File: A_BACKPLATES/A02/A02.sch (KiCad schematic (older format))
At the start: 218 parts, among them J0 Conn_01x01_Male, J1 Conn_01x01_Male, J2 Conn_01x01_Male, J3 Conn_01x01_Male

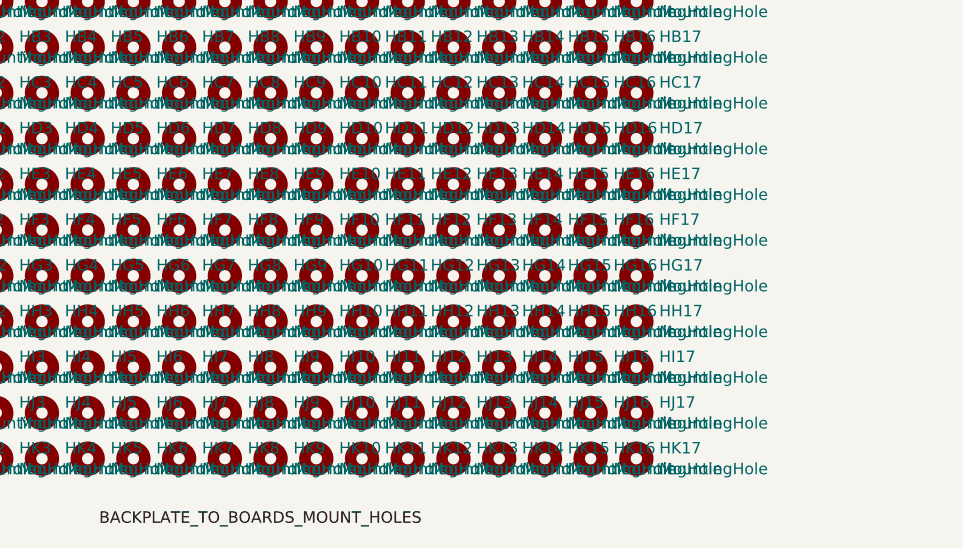
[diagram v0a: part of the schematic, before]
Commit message: A02 all mounting holes placed
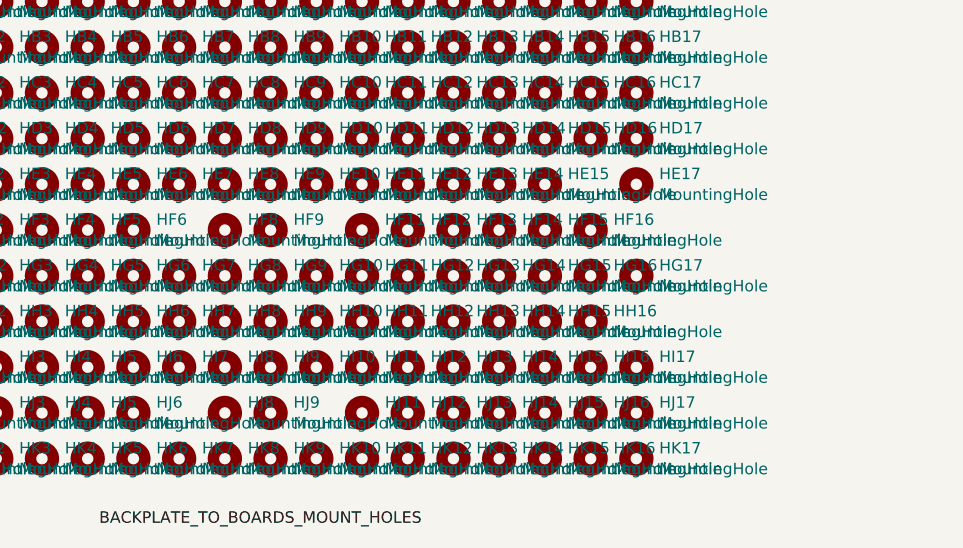
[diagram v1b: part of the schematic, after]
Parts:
- removed HE16, HF10, HF17, HF7, HH17, HJ10, HJ7: MountingHole, MountingHole:MountingHole_3mm, symbol Mechanical:MountingHole
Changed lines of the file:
@@
-$EndComp
-$Comp
-L Mechanical:MountingHole HF7
-U 1 1 5F344477
-P 2200 1700
-F 0 "HF7" H 2300 1746 50  0000 L CNN
-F 1 "MountingHole" H 2300 1655 50  0000 L CNN
-F 2 "MountingHole:MountingHole_3mm" H 2200 1700 50  0001 C CNN
-F 3 "~" H 2200 1700 50  0001 C CNN
-	1    2200 1700
-	1    0    0    -1
 $EndComp
 $Comp
@@
 $EndComp
 $Comp
-L Mechanical:MountingHole HF10
-U 1 1 5F34FFDA
-P 2800 1700
-F 0 "HF10" H 2900 1746 50  0000 L CNN
-F 1 "MountingHole" H 2900 1655 50  0000 L CNN
-F 2 "MountingHole:MountingHole_3mm" H 2800 1700 50  0001 C CNN
-F 3 "~" H 2800 1700 50  0001 C CNN
-	1    2800 1700
-	1    0    0    -1
-$EndComp
-$Comp
 L Mechanical:MountingHole HG10
 U 1 1 5F350A11
@@
 $EndComp
 $Comp
-L Mechanical:MountingHole HE16
-U 1 1 5F36DFE2
-P 4000 1500
-F 0 "HE16" H 4100 1546 50  0000 L CNN
-F 1 "MountingHole" H 4100 1455 50  0000 L CNN
-F 2 "MountingHole:MountingHole_3mm" H 4000 1500 50  0001 C CNN
-F 3 "~" H 4000 1500 50  0001 C CNN
-	1    4000 1500
-	1    0    0    -1
-$EndComp
-$Comp
 L Mechanical:MountingHole HE17
 U 1 1 5F36EE0A
@@
 $EndComp
 $Comp
-L Mechanical:MountingHole HF17
-U 1 1 5F37DE59
-P 4200 1700
-F 0 "HF17" H 4300 1746 50  0000 L CNN
-F 1 "MountingHole" H 4300 1655 50  0000 L CNN
-F 2 "MountingHole:MountingHole_3mm" H 4200 1700 50  0001 C CNN
-F 3 "~" H 4200 1700 50  0001 C CNN
-	1    4200 1700
-	1    0    0    -1
-$EndComp
-$Comp
 L Mechanical:MountingHole HG14
 U 1 1 5F37FA7F
@@
 $EndComp
 $Comp
-L Mechanical:MountingHole HH17
-U 1 1 5F385AD1
-P 4200 2100
-F 0 "HH17" H 4300 2146 50  0000 L CNN
-F 1 "MountingHole" H 4300 2055 50  0000 L CNN
-F 2 "MountingHole:MountingHole_3mm" H 4200 2100 50  0001 C CNN
-F 3 "~" H 4200 2100 50  0001 C CNN
-	1    4200 2100
-	1    0    0    -1
-$EndComp
-$Comp
 L Mechanical:MountingHole HI0
 U 1 1 5F386941
@@
 $EndComp
 $Comp
-L Mechanical:MountingHole HJ7
-U 1 1 5F39FC89
-P 2200 2500
-F 0 "HJ7" H 2300 2546 50  0000 L CNN
-F 1 "MountingHole" H 2300 2455 50  0000 L CNN
-F 2 "MountingHole:MountingHole_3mm" H 2200 2500 50  0001 C CNN
-F 3 "~" H 2200 2500 50  0001 C CNN
-	1    2200 2500
-	1    0    0    -1
-$EndComp
-$Comp
 L Mechanical:MountingHole HK7
 U 1 1 5F3A0A12
@@
 	1    0    0    -1
 $EndComp
-$Comp
-L Mechanical:MountingHole HJ10
-U 1 1 5F3A8139
-P 2800 2500
-F 0 "HJ10" H 2900 2546 50  0000 L CNN
-F 1 "MountingHole" H 2900 2455 50  0000 L CNN
-F 2 "MountingHole:MountingHole_3mm" H 2800 2500 50  0001 C CNN
-F 3 "~" H 2800 2500 50  0001 C CNN
-	1    2800 2500
-	1    0    0    -1
-$EndComp

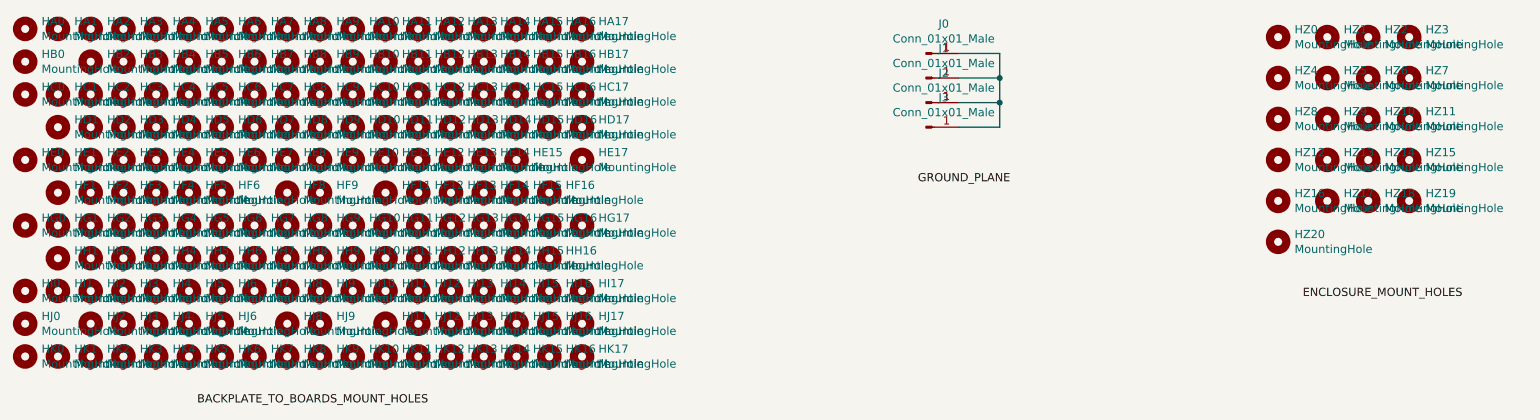
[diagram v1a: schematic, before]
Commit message: edge cuts adjusted
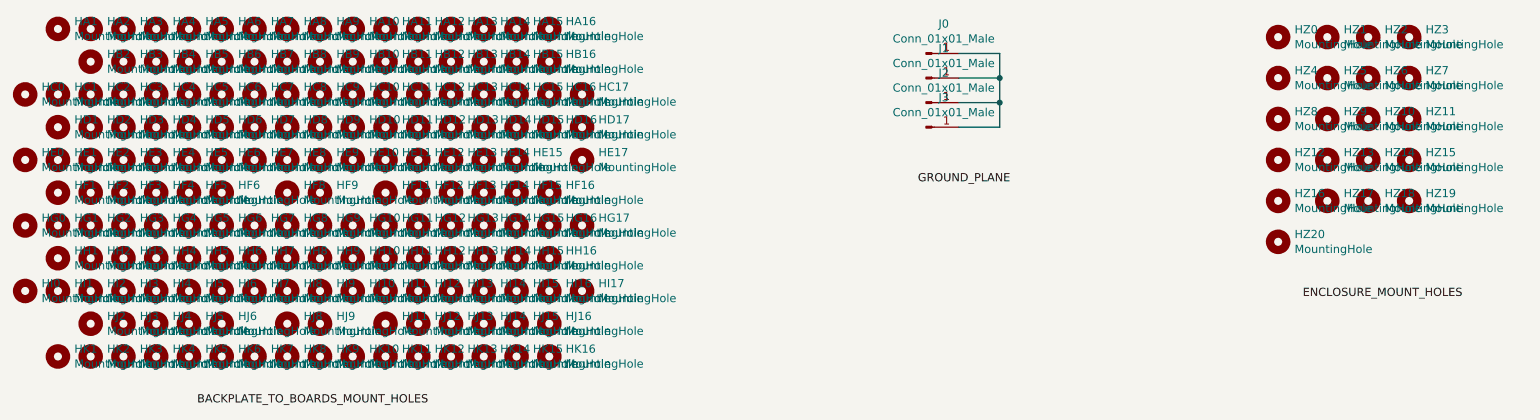
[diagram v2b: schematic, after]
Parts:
- removed HA0, HA17, HB0, HB17, HJ0, HJ17, HK0, HK17: MountingHole, MountingHole:MountingHole_3mm, symbol Mechanical:MountingHole
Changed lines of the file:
@@
 $EndDescr
-$Comp
-L Mechanical:MountingHole HA0
-U 1 1 5F323A1B
-P 800 700
-F 0 "HA0" H 900 746 50  0000 L CNN
-F 1 "MountingHole" H 900 655 50  0000 L CNN
-F 2 "MountingHole:MountingHole_3mm" H 800 700 50  0001 C CNN
-F 3 "~" H 800 700 50  0001 C CNN
-	1    800  700
-	1    0    0    -1
-$EndComp
 $Comp
 L Mechanical:MountingHole HA1
@@
 $EndComp
 $Comp
-L Mechanical:MountingHole HB0
-U 1 1 5F3277F5
-P 800 900
-F 0 "HB0" H 900 946 50  0000 L CNN
-F 1 "MountingHole" H 900 855 50  0000 L CNN
-F 2 "MountingHole:MountingHole_3mm" H 800 900 50  0001 C CNN
-F 3 "~" H 800 900 50  0001 C CNN
-	1    800  900
-	1    0    0    -1
-$EndComp
-$Comp
 L Mechanical:MountingHole HC0
 U 1 1 5F327B1C
@@
 $EndComp
 $Comp
-L Mechanical:MountingHole HA17
-U 1 1 5F35BE54
-P 4200 700
-F 0 "HA17" H 4300 746 50  0000 L CNN
-F 1 "MountingHole" H 4300 655 50  0000 L CNN
-F 2 "MountingHole:MountingHole_3mm" H 4200 700 50  0001 C CNN
-F 3 "~" H 4200 700 50  0001 C CNN
-	1    4200 700
-	1    0    0    -1
-$EndComp
-$Comp
 L Mechanical:MountingHole HB14
 U 1 1 5F362692
@@
 $EndComp
 $Comp
-L Mechanical:MountingHole HB17
-U 1 1 5F364BC1
-P 4200 900
-F 0 "HB17" H 4300 946 50  0000 L CNN
-F 1 "MountingHole" H 4300 855 50  0000 L CNN
-F 2 "MountingHole:MountingHole_3mm" H 4200 900 50  0001 C CNN
-F 3 "~" H 4200 900 50  0001 C CNN
-	1    4200 900
-	1    0    0    -1
-$EndComp
-$Comp
 L Mechanical:MountingHole HC14
 U 1 1 5F365F49
@@
 $EndComp
 $Comp
-L Mechanical:MountingHole HJ0
-U 1 1 5F38B1AB
-P 800 2500
-F 0 "HJ0" H 900 2546 50  0000 L CNN
-F 1 "MountingHole" H 900 2455 50  0000 L CNN
-F 2 "MountingHole:MountingHole_3mm" H 800 2500 50  0001 C CNN
-F 3 "~" H 800 2500 50  0001 C CNN
-	1    800  2500
-	1    0    0    -1
-$EndComp
-$Comp
 L Mechanical:MountingHole HI1
 U 1 1 5F39554D
@@
 $EndComp
 $Comp
-L Mechanical:MountingHole HK0
-U 1 1 5F38B8C6
-P 800 2700
-F 0 "HK0" H 900 2746 50  0000 L CNN
-F 1 "MountingHole" H 900 2655 50  0000 L CNN
-F 2 "MountingHole:MountingHole_3mm" H 800 2700 50  0001 C CNN
-F 3 "~" H 800 2700 50  0001 C CNN
-	1    800  2700
-	1    0    0    -1
-$EndComp
-$Comp
 L Mechanical:MountingHole HK1
 U 1 1 5F396E4D
@@
 $EndComp
 $Comp
-L Mechanical:MountingHole HJ17
-U 1 1 5F3B5211
-P 4200 2500
-F 0 "HJ17" H 4300 2546 50  0000 L CNN
-F 1 "MountingHole" H 4300 2455 50  0000 L CNN
-F 2 "MountingHole:MountingHole_3mm" H 4200 2500 50  0001 C CNN
-F 3 "~" H 4200 2500 50  0001 C CNN
-	1    4200 2500
-	1    0    0    -1
-$EndComp
-$Comp
 L Mechanical:MountingHole HK11
 U 1 1 5F3B5E81
@@
 	1    0    0    -1
 $EndComp
-$Comp
-L Mechanical:MountingHole HK17
-U 1 1 5F3BAA50
-P 4200 2700
-F 0 "HK17" H 4300 2746 50  0000 L CNN
-F 1 "MountingHole" H 4300 2655 50  0000 L CNN
-F 2 "MountingHole:MountingHole_3mm" H 4200 2700 50  0001 C CNN
-F 3 "~" H 4200 2700 50  0001 C CNN
-	1    4200 2700
-	1    0    0    -1
-$EndComp
